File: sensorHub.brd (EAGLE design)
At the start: 160 x 100 mm, 0 parts

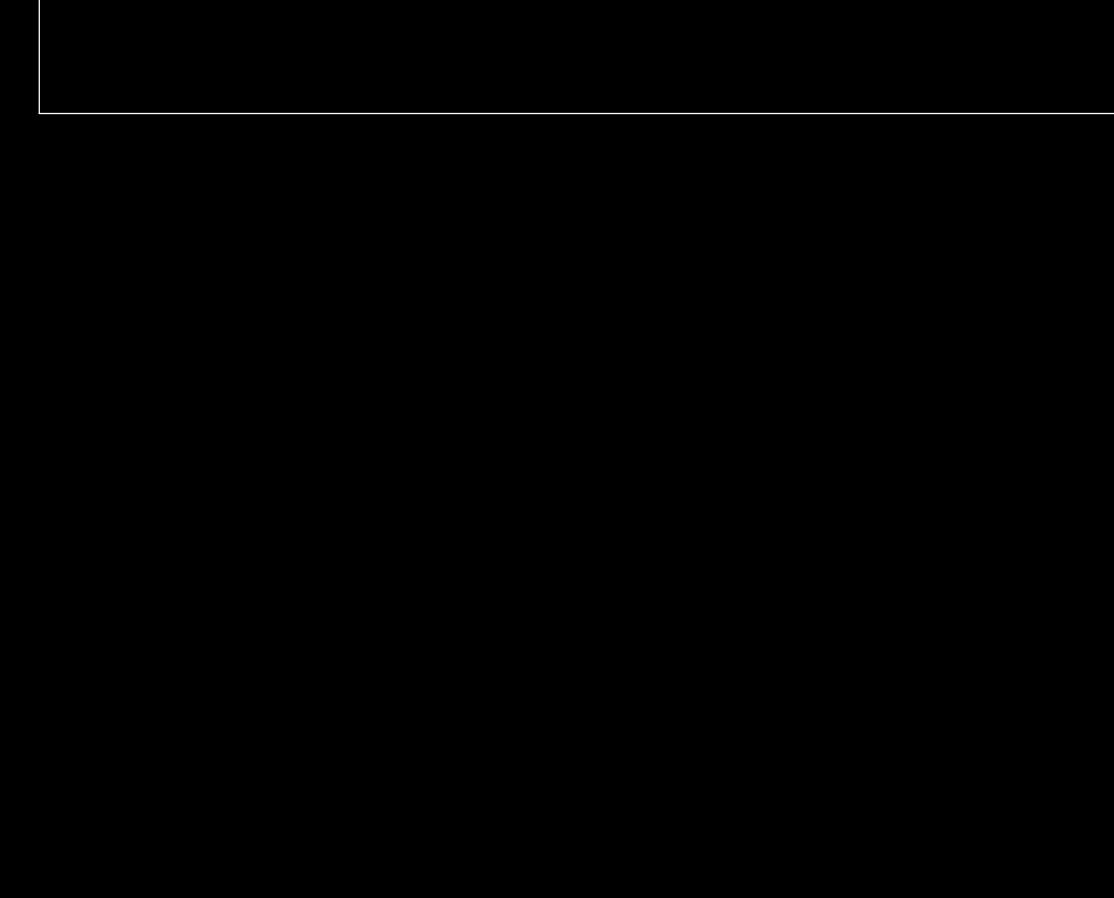
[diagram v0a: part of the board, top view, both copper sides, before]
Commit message: Adds the feather m0 to schematic
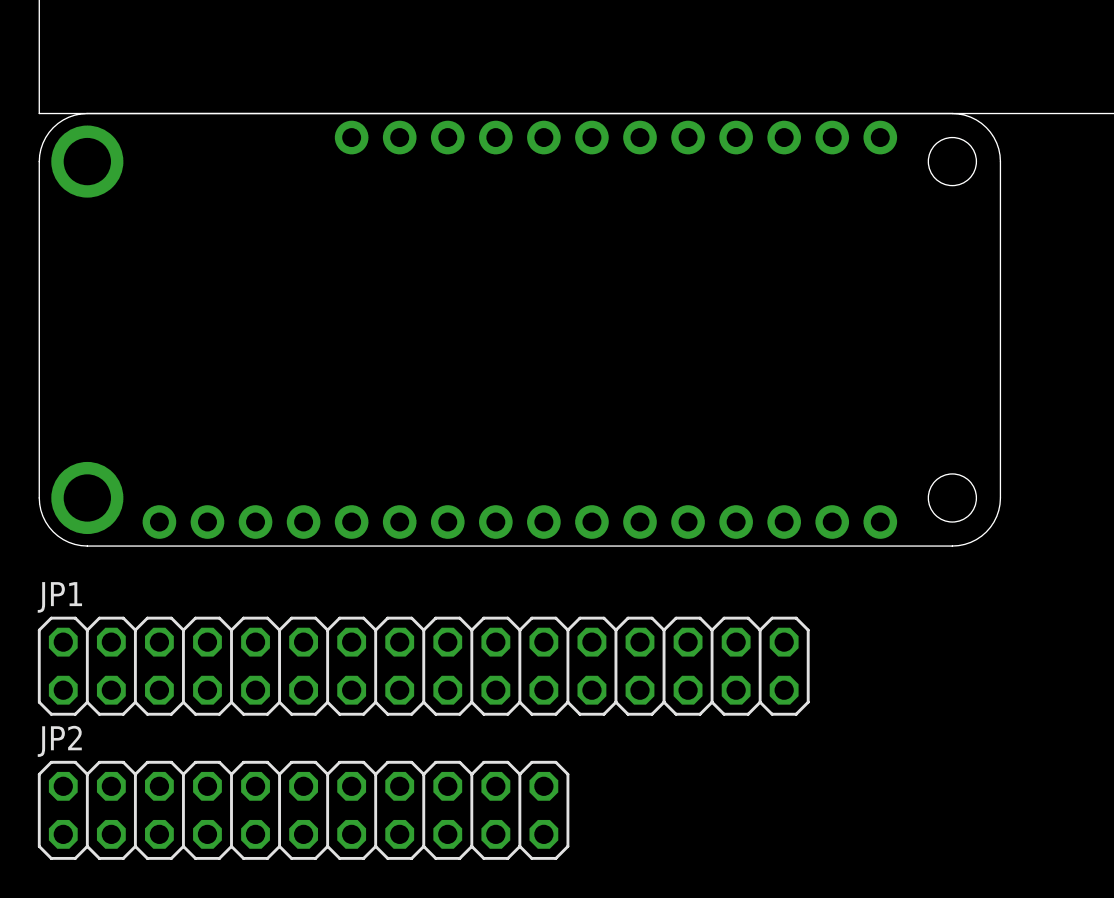
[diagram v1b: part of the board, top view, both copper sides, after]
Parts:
- added JP1: (no value), pinhead:2X16
- added JP2: (no value), pinhead:2X11
- added MS1: FEATHERWING, adafruit:FEATHERWING
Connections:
- new net GND: MS1.4

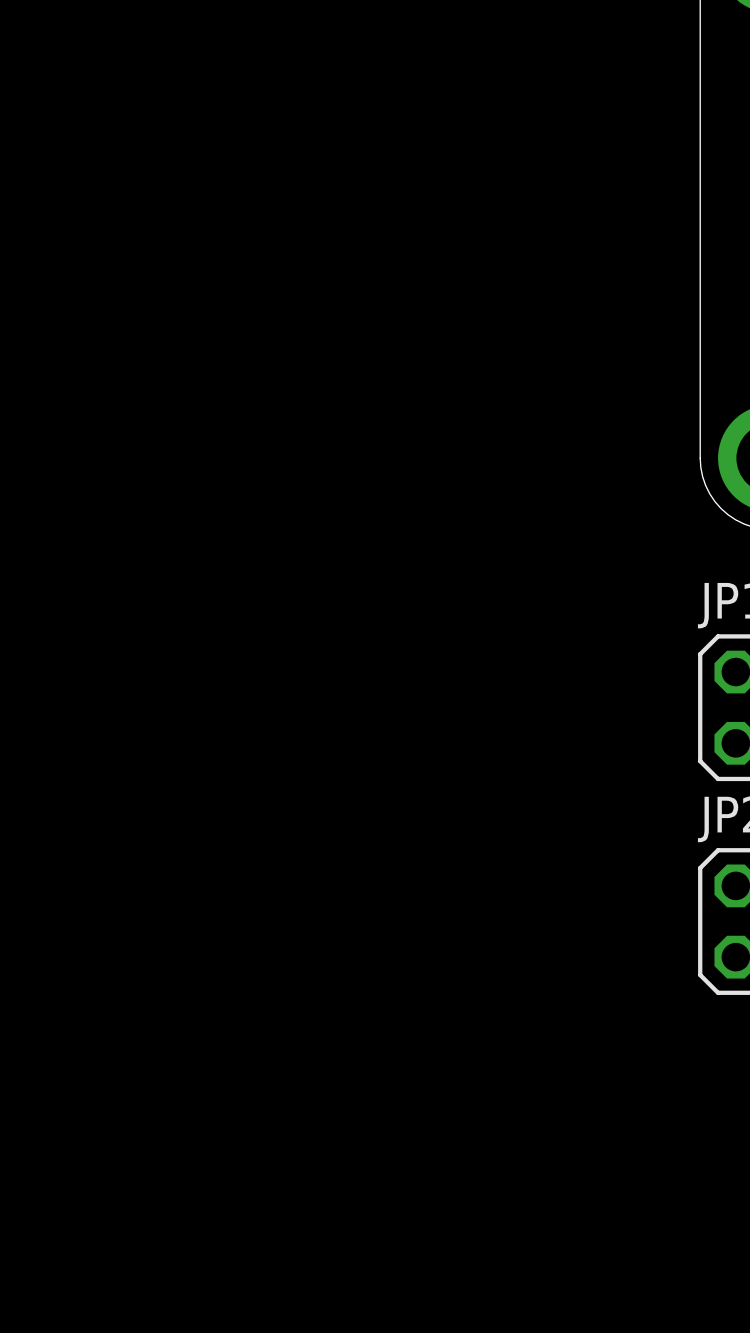
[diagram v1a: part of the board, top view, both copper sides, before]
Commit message: Adds the lm2577 and two pull up resistors to the shematic
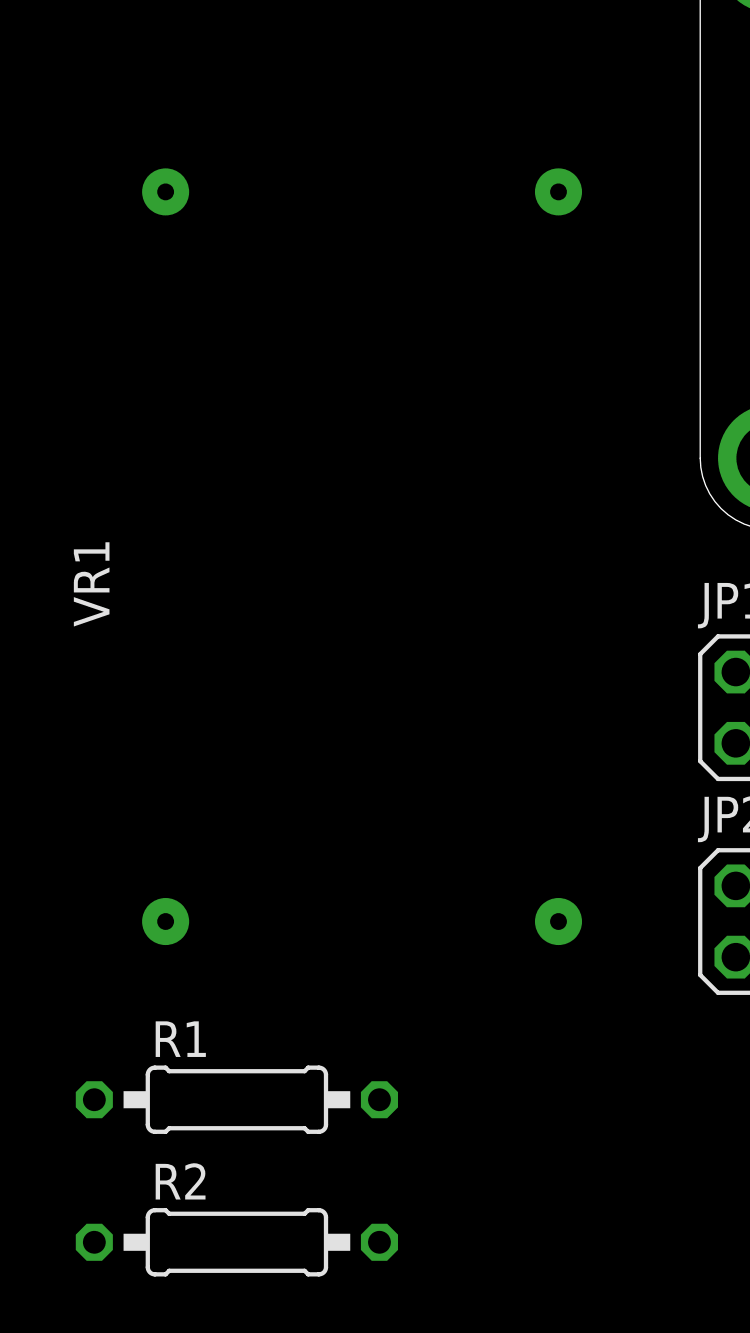
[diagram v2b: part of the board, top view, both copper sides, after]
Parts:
- added R1, R2: (no value), resistor:0207/10
- added VR1: (no value), lm2577_module:MT3608
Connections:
- new net OUT+: VR1.OUT+
- new net OUT-: VR1.OUT-
- new net VIN+: VR1.VIN+
- new net VIN-: VR1.VIN-
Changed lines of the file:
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@@
 <attribute name="VALUE" x="0" y="-41.275" size="1.27" layer="27"/>
+</element>
+<element name="VR1" library="lm2577_module" package="MT3608" value="" x="-19.05" y="-36.83" smashed="yes">
+<attribute name="NAME" x="-21.05" y="-26.33" size="1.27" layer="25" rot="R90"/>
+<attribute name="VALUE" x="-2.05" y="-26.83" size="1.27" layer="27" rot="R90"/>
+</element>
+<element name="R1" library="resistor" library_urn="urn:adsk.eagle:library:348" package="0207/10" package3d_urn="urn:adsk.eagle:package:25939/1" value="" x="-16.51" y="-43.18" smashed="yes">
+<attribute name="NAME" x="-19.558" y="-41.656" size="1.27" layer="25" ratio="10"/>
+<attribute name="VALUE" x="-18.7706" y="-43.815" size="1.27" layer="27" ratio="10"/>
+</element>
+<element name="R2" library="resistor" library_urn="urn:adsk.eagle:library:348" package="0207/10" package3d_urn="urn:adsk.eagle:package:25939/1" value="" x="-16.51" y="-48.26" smashed="yes">
+<attribute name="NAME" x="-19.558" y="-46.736" size="1.27" layer="25" ratio="10"/>
+<attribute name="VALUE" x="-18.7706" y="-48.895" size="1.27" layer="27" ratio="10"/>
 </element>
 </elements>
@@
 <contactref element="MS1" pad="4"/>
 </signal>
+<signal name="VIN+">
+<contactref element="VR1" pad="VIN+"/>
+</signal>
+<signal name="VIN-">
+<contactref element="VR1" pad="VIN-"/>
+</signal>
+<signal name="OUT+">
+<contactref element="VR1" pad="OUT+"/>
+</signal>
+<signal name="OUT-">
+<contactref element="VR1" pad="OUT-"/>
+</signal>
 </signals>

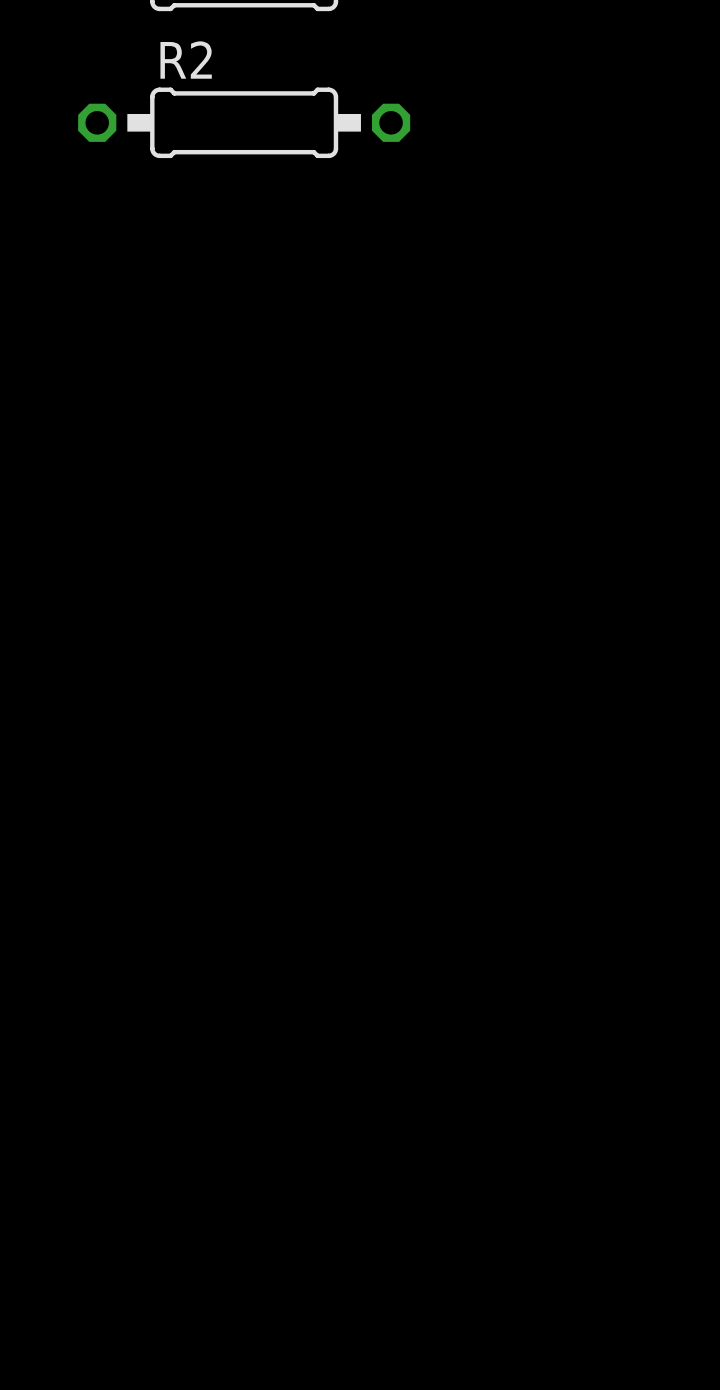
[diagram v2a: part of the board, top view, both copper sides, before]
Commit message: Adds connector pins for the sensors to the schematic
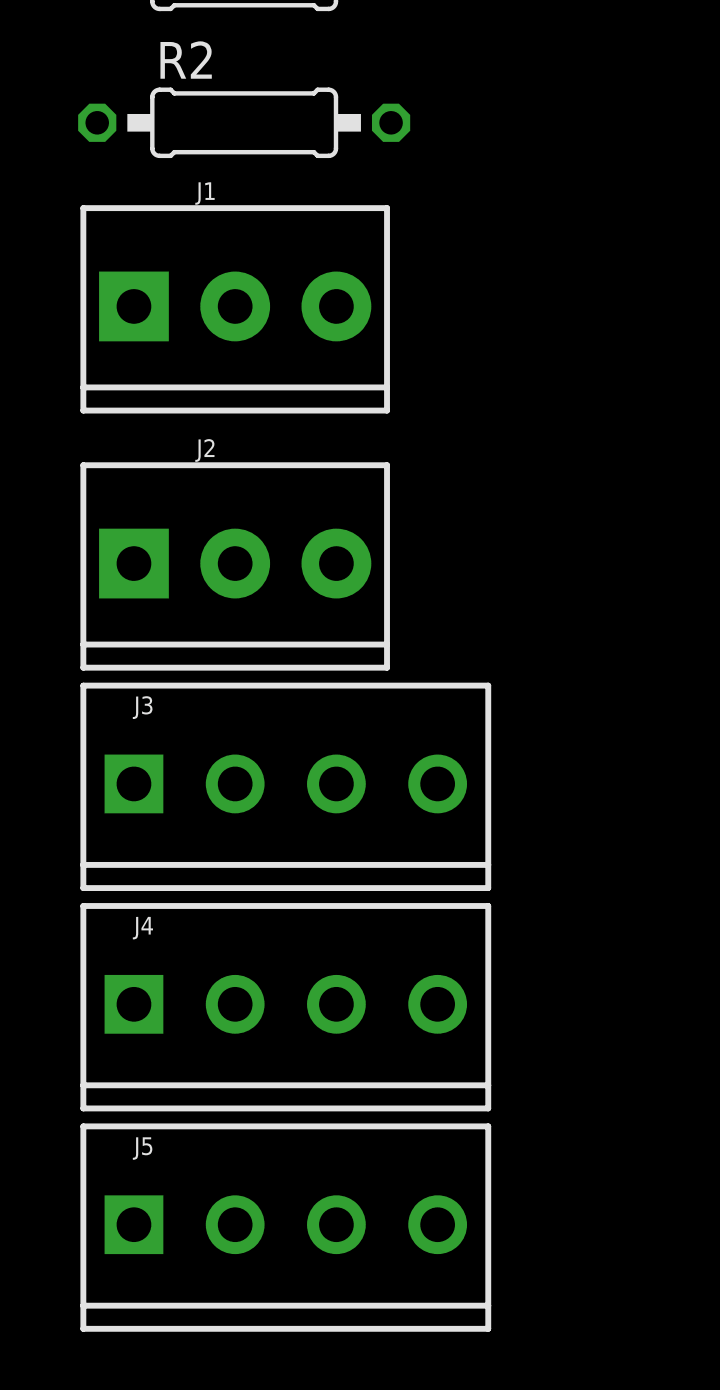
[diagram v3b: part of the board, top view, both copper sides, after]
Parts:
- added J1, J2: (no value), SparkFun-Connectors:SCREWTERMINAL-3.5MM-3
- added J3, J4, J5: (no value), SparkFun-Connectors:SCREWTERMINAL-3.5MM-4
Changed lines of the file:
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@@
 <layer number="112" name="tSilk" color="7" fill="1" visible="no" active="yes"/>
 <layer number="113" name="ReferenceLS" color="7" fill="1" visible="no" active="no"/>
+<layer number="114" name="Badge_Outline" color="7" fill="1" visible="yes" active="yes"/>
+<layer number="115" name="ReferenceISLANDS" color="7" fill="1" visible="yes" active="yes"/>
 <layer number="116" name="Patch_BOT" color="9" fill="4" visible="no" active="yes"/>
 <layer number="118" name="Rect_Pads" color="7" fill="1" visible="no" active="no"/>
@@
 <attribute name="VALUE" x="-18.7706" y="-48.895" size="1.27" layer="27" ratio="10"/>
 </element>
+<element name="J1" library="SparkFun-Connectors" package="SCREWTERMINAL-3.5MM-3" value="" x="-20.32" y="-54.61" smashed="yes">
+<attribute name="NAME" x="-18.161" y="-50.927" size="0.6096" layer="25" font="vector" ratio="20"/>
+<attribute name="PROD_ID" value="CONN-08288" x="-20.32" y="-54.61" size="1.778" layer="27" display="off"/>
+<attribute name="SF_ID" value="PRT-08235" x="-20.32" y="-54.61" size="1.778" layer="27" display="off"/>
+<attribute name="VALUE" x="-18.288" y="-59.182" size="0.6096" layer="27" font="vector" ratio="20"/>
+</element>
+<element name="J2" library="SparkFun-Connectors" package="SCREWTERMINAL-3.5MM-3" value="" x="-20.32" y="-63.5" smashed="yes">
+<attribute name="NAME" x="-18.161" y="-59.817" size="0.6096" layer="25" font="vector" ratio="20"/>
+<attribute name="PROD_ID" value="CONN-08288" x="-20.32" y="-63.5" size="1.778" layer="27" display="off"/>
+<attribute name="SF_ID" value="PRT-08235" x="-20.32" y="-63.5" size="1.778" layer="27" display="off"/>
+<attribute name="VALUE" x="-18.288" y="-68.072" size="0.6096" layer="27" font="vector" ratio="20"/>
+</element>
+<element name="J3" library="SparkFun-Connectors" package="SCREWTERMINAL-3.5MM-4" value="" x="-20.32" y="-71.12" smashed="yes">
+<attribute name="NAME" x="-20.32" y="-68.707" size="0.6096" layer="25" font="vector" ratio="20"/>
+<attribute name="PROD_ID" value="2xCONN-08399" x="-20.32" y="-71.12" size="1.778" layer="27" display="off"/>
+<attribute name="SF_ID" value="2xPRT-08084" x="-20.32" y="-71.12" size="1.778" layer="27" display="off"/>
+<attribute name="VALUE" x="-20.32" y="-73.406" size="0.6096" layer="27" font="vector" ratio="20"/>
+</element>
+<element name="J4" library="SparkFun-Connectors" package="SCREWTERMINAL-3.5MM-4" value="" x="-20.32" y="-78.74" smashed="yes">
+<attribute name="NAME" x="-20.32" y="-76.327" size="0.6096" layer="25" font="vector" ratio="20"/>
+<attribute name="PROD_ID" value="2xCONN-08399" x="-20.32" y="-78.74" size="1.778" layer="27" display="off"/>
+<attribute name="SF_ID" value="2xPRT-08084" x="-20.32" y="-78.74" size="1.778" layer="27" display="off"/>
+<attribute name="VALUE" x="-20.32" y="-81.026" size="0.6096" layer="27" font="vector" ratio="20"/>
+</element>
+<element name="J5" library="SparkFun-Connectors" package="SCREWTERMINAL-3.5MM-4" value="" x="-20.32" y="-86.36" smashed="yes">
+<attribute name="NAME" x="-20.32" y="-83.947" size="0.6096" layer="25" font="vector" ratio="20"/>
+<attribute name="PROD_ID" value="2xCONN-08399" x="-20.32" y="-86.36" size="1.778" layer="27" display="off"/>
+<attribute name="SF_ID" value="2xPRT-08084" x="-20.32" y="-86.36" size="1.778" layer="27" display="off"/>
+<attribute name="VALUE" x="-20.32" y="-88.646" size="0.6096" layer="27" font="vector" ratio="20"/>
+</element>
 </elements>
